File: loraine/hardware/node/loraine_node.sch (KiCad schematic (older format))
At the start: 43 parts, among them CON1 BARREL_JACK, IC1 ATTINY2313A-S, P1 POWER_THRU, P2 POWER, P3 SOLDER_PAD, P4 ICSP, P5 OUTPUTS, P6 BUS, P7 BUS_THRU, Q1 BD679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

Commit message: Split project into node and uplighter
Node now contains ATTINY, bus controller and most logic and programing

Uplighter board is just three LEDs and their drivers (and sense resistors)

Connection between the two is currently a SIL9 but might be better split into three (or so) connectors so the connectors can stably mount the uplighter board.
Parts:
- removed D1: RED, symbol LED
- removed D2: GREEN, symbol LED
- removed D3: BLUE, symbol LED
- removed R1, R2, R3: 0.47R 0.25W, symbol R
- removed U3, U4, U5: TL4242, symbol TL4242
- added P8: CONN_9, symbol CONN_9
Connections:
- wire segments 188 -> 152

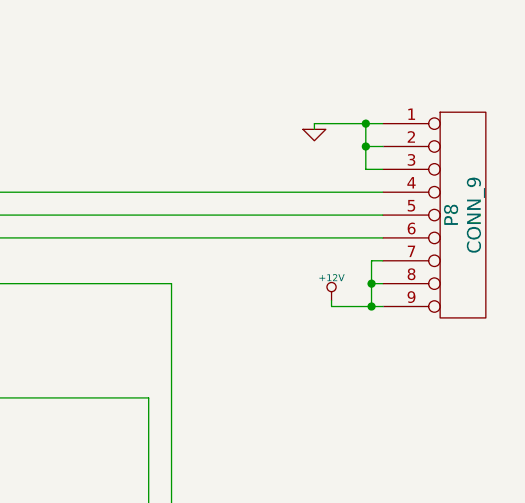
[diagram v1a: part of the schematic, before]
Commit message: Split board-board connector to 3x SIL3
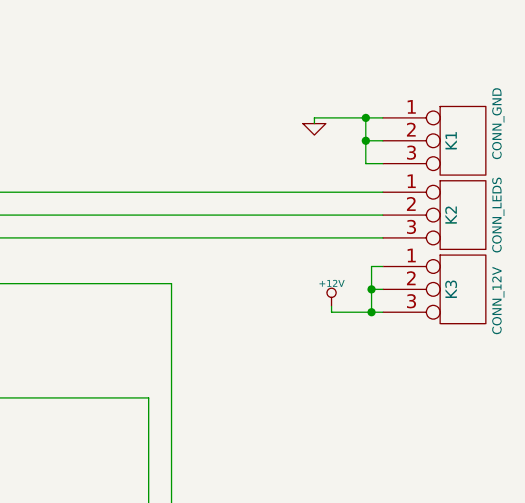
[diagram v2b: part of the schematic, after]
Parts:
- removed P8: CONN_9, symbol CONN_9
- added K1: CONN_GND, symbol CONN_3
- added K2: CONN_LEDS, symbol CONN_3
- added K3: CONN_12V, symbol CONN_3
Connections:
- net +12V: now also K3.1 (P1), K3.2 (PM), K3.3 (P3)
- net GND: now also K1.1 (P1), K1.2 (PM), K1.3 (P3)
- net at IC1.12 ((PCINT0/AIN0)PB0), R4.2: now also K2.1 (P1)
- net at IC1.13 ((PCINT1/AIN1)PB1), R5.2: now also K2.2 (PM)
- net at IC1.14 ((PCINT2/OC0A)PB2), R6.2: now also K2.3 (P3)
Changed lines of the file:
@@
 $EndComp
 $Comp
-L GND #PWR10
+L GND #PWR01
 U 1 1 5338784C
 P 1200 4750
-F 0 "#PWR10" H 1200 4750 30  0001 C CNN
+F 0 "#PWR01" H 1200 4750 30  0001 C CNN
 F 1 "GND" H 1200 4680 30  0001 C CNN
 F 2 "" H 1200 4750 60  0000 C CNN
@@
 $EndComp
 $Comp
-L GND #PWR4
+L GND #PWR02
 U 1 1 533879F1
 P 3850 1650
-F 0 "#PWR4" H 3850 1650 30  0001 C CNN
+F 0 "#PWR02" H 3850 1650 30  0001 C CNN
 F 1 "GND" H 3850 1580 30  0001 C CNN
 F 2 "" H 3850 1650 60  0000 C CNN
@@
 $EndComp
 $Comp
-L GND #PWR12
+L GND #PWR03
 U 1 1 53388767
 P 7000 6150
-F 0 "#PWR12" H 7000 6150 30  0001 C CNN
+F 0 "#PWR03" H 7000 6150 30  0001 C CNN
 F 1 "GND" H 7000 6080 30  0001 C CNN
 F 2 "" H 7000 6150 60  0000 C CNN
@@
 $EndComp
 $Comp
-L GND #PWR15
+L GND #PWR04
 U 1 1 53388FDD
 P 4750 7250
-F 0 "#PWR15" H 4750 7250 30  0001 C CNN
+F 0 "#PWR04" H 4750 7250 30  0001 C CNN
 F 1 "GND" H 4750 7180 30  0001 C CNN
 F 2 "" H 4750 7250 60  0000 C CNN
@@
 $EndComp
 $Comp
-L GND #PWR9
+L GND #PWR05
 U 1 1 5338AC70
 P 3900 3350
-F 0 "#PWR9" H 3900 3350 30  0001 C CNN
+F 0 "#PWR05" H 3900 3350 30  0001 C CNN
 F 1 "GND" H 3900 3280 30  0001 C CNN
 F 2 "" H 3900 3350 60  0000 C CNN
@@
 $EndComp
 $Comp
-L GND #PWR11
+L GND #PWR06
 U 1 1 5338F7A1
 P 3450 5500
-F 0 "#PWR11" H 3450 5500 30  0001 C CNN
+F 0 "#PWR06" H 3450 5500 30  0001 C CNN
 F 1 "GND" H 3450 5430 30  0001 C CNN
 F 2 "" H 3450 5500 60  0000 C CNN
@@
 $EndComp
 $Comp
-L GND #PWR7
+L GND #PWR07
 U 1 1 5338FB33
 P 5700 3050
-F 0 "#PWR7" H 5700 3050 30  0001 C CNN
+F 0 "#PWR07" H 5700 3050 30  0001 C CNN
 F 1 "GND" H 5700 2980 30  0001 C CNN
 F 2 "" H 5700 3050 60  0000 C CNN
@@
 $EndComp
 $Comp
-L GND #PWR16
+L GND #PWR08
 U 1 1 5338FCA4
 P 3200 7350
-F 0 "#PWR16" H 3200 7350 30  0001 C CNN
+F 0 "#PWR08" H 3200 7350 30  0001 C CNN
 F 1 "GND" H 3200 7280 30  0001 C CNN
 F 2 "" H 3200 7350 60  0000 C CNN
@@
 $EndComp
 $Comp
-L +12V #PWR1
+L +12V #PWR09
 U 1 1 5339006C
 P 2200 1100
-F 0 "#PWR1" H 2200 1050 20  0001 C CNN
+F 0 "#PWR09" H 2200 1050 20  0001 C CNN
 F 1 "+12V" H 2200 1200 30  0000 C CNN
 F 2 "" H 2200 1100 60  0000 C CNN
@@
 $EndComp
 $Comp
-L VCC #PWR2
+L VCC #PWR010
 U 1 1 53390080
 P 3850 1100
-F 0 "#PWR2" H 3850 1200 30  0001 C CNN
+F 0 "#PWR010" H 3850 1200 30  0001 C CNN
 F 1 "VCC" H 3850 1200 30  0000 C CNN
 F 2 "" H 3850 1100 60  0000 C CNN
@@
 $EndComp
 $Comp
-L VCC #PWR8
+L VCC #PWR011
 U 1 1 53390544
 P 3450 3150
-F 0 "#PWR8" H 3450 3250 30  0001 C CNN
+F 0 "#PWR011" H 3450 3250 30  0001 C CNN
 F 1 "VCC" H 3450 3250 30  0000 C CNN
 F 2 "" H 3450 3150 60  0000 C CNN
@@
 $EndComp
 $Comp
-L VCC #PWR6
+L VCC #PWR012
 U 1 1 5339060A
 P 5600 2750
-F 0 "#PWR6" H 5600 2850 30  0001 C CNN
+F 0 "#PWR012" H 5600 2850 30  0001 C CNN
 F 1 "VCC" H 5600 2850 30  0000 C CNN
 F 2 "" H 5600 2750 60  0000 C CNN
@@
 $EndComp
 $Comp
-L VCC #PWR13
+L VCC #PWR013
 U 1 1 5339091E
 P 3200 6800
-F 0 "#PWR13" H 3200 6900 30  0001 C CNN
+F 0 "#PWR013" H 3200 6900 30  0001 C CNN
 F 1 "VCC" H 3200 6900 30  0000 C CNN
 F 2 "" H 3200 6800 60  0000 C CNN
@@
 $EndComp
 $Comp
-L GND #PWR14
+L GND #PWR014
 U 1 1 5339D1EB
 P 2700 6900
-F 0 "#PWR14" H 2700 6900 30  0001 C CNN
+F 0 "#PWR014" H 2700 6900 30  0001 C CNN
 F 1 "GND" H 2700 6830 30  0001 C CNN
 F 2 "" H 2700 6900 60  0000 C CNN
@@
 	6000 1700 8875 1700
 $Comp
-L CONN_9 P8
-U 1 1 536EB293
+L GND #PWR015
+U 1 1 536EB852
+P 8575 1400
+F 0 "#PWR015" H 8575 1400 30  0001 C CNN
+F 1 "GND" H 8575 1330 30  0001 C CNN
+F 2 "" H 8575 1400 60  0000 C CNN
+F 3 "" H 8575 1400 60  0000 C CNN
+	1    8575 1400
+	1    0    0    -1
+$EndComp
+Wire Wire Line
+	8575 1400 8575 1375
+Wire Wire Line
+	8575 1375 8875 1375
+Wire Wire Line
+	8800 1375 8800 1575
+Wire Wire Line
+	8800 1475 8875 1475
+Connection ~ 8800 1375
+Wire Wire Line
+	8800 1575 8875 1575
+Connection ~ 8800 1475
+$Comp
+L +12V #PWR016
+U 1 1 536EBC0F
+P 8650 2200
+F 0 "#PWR016" H 8650 2150 20  0001 C CNN
+F 1 "+12V" H 8650 2300 30  0000 C CNN
+F 2 "" H 8650 2200 60  0000 C CNN
+F 3 "" H 8650 2200 60  0000 C CNN
+	1    8650 2200
+	1    0    0    -1
+$EndComp
+Wire Wire Line
+	8650 2200 8650 2225
+Wire Wire Line
+	8650 2225 8875 2225
+Wire Wire Line
+	8825 2025 8825 2225
+Wire Wire Line
+	8825 2125 8875 2125
+Connection ~ 8825 2225
+Wire Wire Line
+	8825 2025 8875 2025
+Connection ~ 8825 2125
+$Comp
+L CONN_3 K1
+U 1 1 536EA170
+P 9225 1475
+F 0 "K1" V 9175 1475 50  0000 C CNN
+F 1 "CONN_GND" V 9375 1550 40  0000 C CNN
+F 2 "" H 9225 1475 60  0000 C CNN
+F 3 "" H 9225 1475 60  0000 C CNN
+	1    9225 1475
+	1    0    0    -1
+$EndComp
+$Comp
+L CONN_3 K2
+U 1 1 536EA1BC
 P 9225 1800
-F 0 "P8" V 9175 1800 60  0000 C CNN
-F 1 "CONN_9" V 9275 1800 60  0000 C CNN
+F 0 "K2" V 9175 1800 50  0000 C CNN
+F 1 "CONN_LEDS" V 9375 1800 40  0000 C CNN
 F 2 "" H 9225 1800 60  0000 C CNN
 F 3 "" H 9225 1800 60  0000 C CNN
@@
 $EndComp
 $Comp
-L GND #PWR3
-U 1 1 536EB852
-P 8575 1425
-F 0 "#PWR3" H 8575 1425 30  0001 C CNN
-F 1 "GND" H 8575 1355 30  0001 C CNN
-F 2 "" H 8575 1425 60  0000 C CNN
-F 3 "" H 8575 1425 60  0000 C CNN
-	1    8575 1425
-	1    0    0    -1
-$EndComp
-Wire Wire Line
-	8575 1425 8575 1400
-Wire Wire Line
-	8575 1400 8875 1400
-Wire Wire Line
-	8800 1400 8800 1600
-Wire Wire Line
-	8800 1500 8875 1500
-Connection ~ 8800 1400
-Wire Wire Line
-	8800 1600 8875 1600
-Connection ~ 8800 1500
-$Comp
-L +12V #PWR5
-U 1 1 536EBC0F
-P 8650 2175
-F 0 "#PWR5" H 8650 2125 20  0001 C CNN
-F 1 "+12V" H 8650 2275 30  0000 C CNN
-F 2 "" H 8650 2175 60  0000 C CNN
-F 3 "" H 8650 2175 60  0000 C CNN
-	1    8650 2175
-	1    0    0    -1
-$EndComp
-Wire Wire Line
-	8650 2175 8650 2200
-Wire Wire Line
-	8650 2200 8875 2200
-Wire Wire Line
-	8825 2000 8825 2200
-Wire Wire Line
-	8825 2100 8875 2100
-Connection ~ 8825 2200
-Wire Wire Line
-	8825 2000 8875 2000
-Connection ~ 8825 2100
+L CONN_3 K3
+U 1 1 536EA1FB
+P 9225 2125
+F 0 "K3" V 9175 2125 50  0000 C CNN
+F 1 "CONN_12V" V 9375 2075 40  0000 C CNN
+F 2 "" H 9225 2125 60  0000 C CNN
+F 3 "" H 9225 2125 60  0000 C CNN
+	1    9225 2125
+	1    0    0    -1
+$EndComp
 $EndSCHEMATC
